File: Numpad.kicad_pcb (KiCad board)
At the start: 2 copper layers, 50 parts, among them J1 USB_B_Mini, SW0 MXSwitch, SW1 MXSwitch, SW2 MXSwitch, SW3 MXSwitch, SW4 MXSwitch, SW5 MXSwitch, SW6 MXSwitch, SW7 MXSwitch, SW8 MXSwitch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

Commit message: Components roughly placed in grid, connected rows and cols to processor
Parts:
- moved SWPls1 171.3 mm to (256.5, 80.6)
- moved SWEnt1 171.2 mm to (256.5, 118.7)
- moved C4 167.6 mm to (65.4, -31.1)
- moved C1 134.6 mm to (102.9, -24.1)
- moved C2 134.6 mm to (97.1, -17.4)
- moved C3 134.6 mm to (128.7, -49.6)
- moved C5 134.6 mm to (139.8, -61.1)
- moved C6 134.6 mm to (123.0, -42.9)
- moved C7 134.6 mm to (162.2, -81.2)
- moved J1 134.6 mm to (126.2, -63.5)
- moved R1 134.6 mm to (20.9, -1.16)
- moved R2 134.6 mm to (52.6, -1.91)
- moved R3 134.6 mm to (46.7, -1.91)
- moved R4 134.6 mm to (40.7, -1.91)
- moved SWRst1 134.6 mm to (33.0, -4.28)
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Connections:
- U1 pad 10: Net-(U1-Pad10) -> Row3
- U1 pad 11: Net-(U1-Pad11) -> Row4
- U1 pad 18: Net-(U1-Pad18) -> Col1
- U1 pad 19: Net-(U1-Pad19) -> Col2
- U1 pad 20: Net-(U1-Pad20) -> Col3
- U1 pad 21: Net-(U1-Pad21) -> Col4
- U1 pad 28: Net-(U1-Pad28) -> Row5
- U1 pad 8: Net-(U1-Pad8) -> Row1
- U1 pad 9: Net-(U1-Pad9) -> Row2

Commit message: components roughly placed
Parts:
- added H1: MountingHole, MountingHole:MountingHole_3mm_Pad, F.Cu at (189.9, 61.6)
- added H2: MountingHole, MountingHole:MountingHole_3mm_Pad, F.Cu at (189.9, 118.7)
- added H3: MountingHole, MountingHole:MountingHole_3mm_Pad, F.Cu at (228.0, 61.6)
- added H4: MountingHole, MountingHole:MountingHole_3mm_Pad, F.Cu at (228.0, 118.7)
- Y1: footprint Crystal:Crystal_SMD_5032-2Pin_5.0x3.2mm_HandSoldering -> Crystal:Crystal_SMD_3225-4Pin_3.2x2.5mm_HandSoldering
- moved SWRst1 221.9 mm to (211.5, 127.6)
- moved Y1 213.4 mm to (208.9, 99.7), turned to 180 degrees
- moved R1 209.2 mm to (182.2, 132.1), turned to 270 degrees
- moved R3 179.0 mm to (214.0, 61.6), turned to 180 degrees
- moved R4 175.6 mm to (204.5, 61.6), turned to 180 degrees
- moved C1 174.4 mm to (177.8, 133.3), turned to 180 degrees
- moved C3 173.9 mm to (208.9, 104.8)
- moved C2 158.3 mm to (208.9, 94.6)
- moved U1 150.2 mm to (180.3, 99.7), turned to 90 degrees
- moved R2 146.8 mm to (180.3, 70.5), turned to 180 degrees
- moved C4 146.1 mm to (190.5, 44.5)
- moved C7 143.9 mm to (207.6, 55.2), turned to 90 degrees
- moved J1 137.5 mm to (208.9, 46.4), turned to 180 degrees
- moved C5 137.3 mm to (212.7, 55.2), turned to 90 degrees
- moved DNum1 134.7 mm to (244.5, 55.2), turned to 90 degrees
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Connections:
- net Net-(R2-Pad1) renamed D+
- net Net-(R3-Pad1) renamed D-
- Y1 pad 2: Net-(C3-Pad1) -> GND

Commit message: ignore bak files, went bak to standard pcb orientation
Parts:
- added R5: 330, Resistor_SMD:R_1206_3216Metric_Pad1.42x1.75mm_HandSolder, F.Cu at (50.8, 58.4)
- D0, D1, D2, D3, D4, D5, D6, D7, D8, D9, DAst1, DDel1, DDiv1, DEnt1, DNum1, DPls1: value D_Small -> 1N4148W
- R4: value 10K -> 1K
- moved C7 191.4 mm to (16.5, 45.7)
- moved SWRst1 191.4 mm to (20.3, 118.1)
- moved C2 191.4 mm to (17.8, 85.1)
- moved C3 191.4 mm to (17.8, 95.2)
- moved C5 191.4 mm to (21.6, 45.7)
- moved C6 191.4 mm to (19.1, 45.7)
- moved C8 191.4 mm to (14.0, 45.7)
- moved D3 191.4 mm to (15.2, 102.9)
- moved J1 191.4 mm to (17.8, 36.8)
- moved R3 191.4 mm to (22.9, 52.1)
- moved R4 191.4 mm to (13.3, 52.1)
- moved Y1 191.4 mm to (17.8, 90.2)
- moved DNum1 151.8 mm to (92.7, 52.7)
- moved DDiv1 149.9 mm to (75.6, 50.2)
- moved D0 143.6 mm to (91.4, 125.7)
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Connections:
- C1 pad 2: GND -> Net-(C1-Pad2)
- SWRst1 pad 2: GND -> Net-(C1-Pad2)

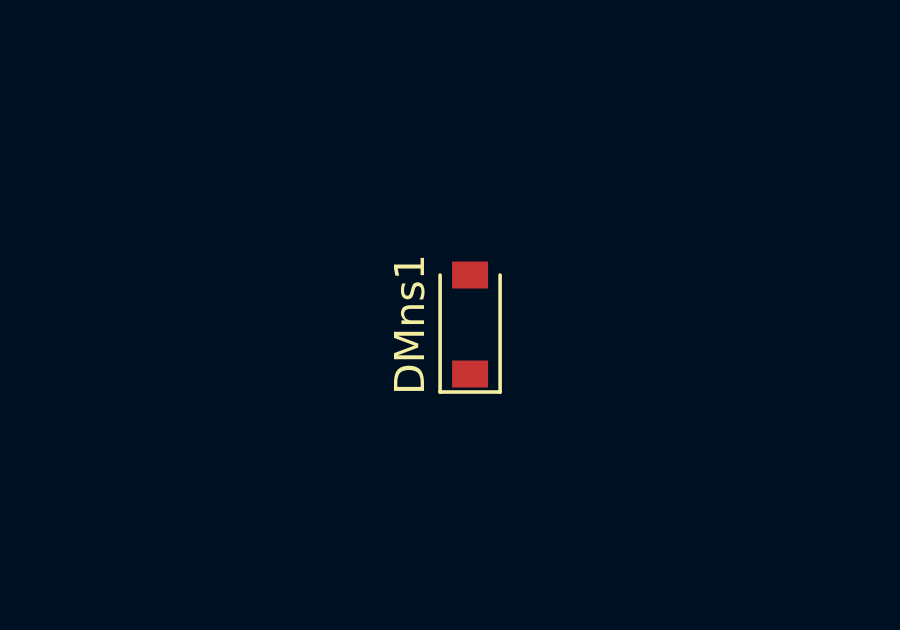
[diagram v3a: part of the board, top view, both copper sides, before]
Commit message: MX labels updated, missed diode spec
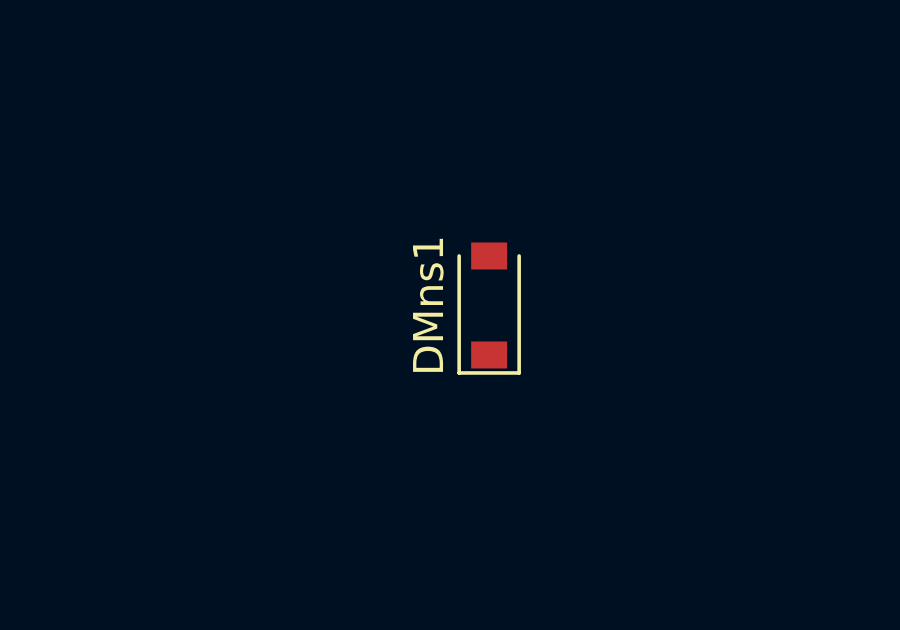
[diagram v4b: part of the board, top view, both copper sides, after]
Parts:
- DMns1: value D_Small -> 1N4148W
- SW0: value MXSwitch -> 0
- SW1: value MXSwitch -> 1
- SW2: value MXSwitch -> 2
- SW3: value MXSwitch -> 3
- SW4: value MXSwitch -> 4
- SW5: value MXSwitch -> 5
- SW6: value MXSwitch -> 6
- SW7: value MXSwitch -> 7
- SW8: value MXSwitch -> 8
- SW9: value MXSwitch -> 9
- SWAst1: value MXSwitch -> *
- SWDel1: value MXSwitch -> Del
- SWDiv1: value MXSwitch -> /
- SWEnt1: value MXSwitch -> Ent
- SWMns1: value MXSwitch -> -
- SWNum1: value MXSwitch -> Num
- SWPls1: value MXSwitch -> +
- moved DMns1 0.90 mm to (123.8, 53.3)
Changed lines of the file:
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@@
   (module AcheronMX:MX200V (layer F.Cu)
     (at 248.92 76.835)
-    (fp_text reference SWPls1 (at 0 3.175) (layer Cmts.User)
-      (effects (font (size 1 1) (thickness 0.15) italic))
-    )
-    (fp_text value MXSwitch (at 0 8.7) (layer Cmts.User)
+    (fp_text reference SWPls1 (at 0 3.175) (layer Cmts.User) hide
+      (effects (font (size 1 1) (thickness 0.15) italic))
+    )
+    (fp_text value + (at 0 8.7) (layer Cmts.User)
       (effects (font (size 1 1) (thickness 0.15)))
     )
@@
   (module AcheronMX:MX100 (layer F.Cu)
     (at 191.77 48.26)
-    (fp_text reference SWNum1 (at 0 3.175) (layer Cmts.User)
-      (effects (font (size 1 1) (thickness 0.15) italic))
-    )
-    (fp_text value MXSwitch (at 0 8.636) (layer Cmts.User)
+    (fp_text reference SWNum1 (at 0 3.175) (layer Cmts.User) hide
+      (effects (font (size 1 1) (thickness 0.15) italic))
+    )
+    (fp_text value Num (at 0 8.636) (layer Cmts.User)
       (effects (font (size 1 1) (thickness 0.15)))
     )
@@
   (module AcheronMX:MX100 (layer F.Cu)
     (at 248.92 48.26)
-    (fp_text reference SWMns1 (at 0 3.175) (layer Cmts.User)
-      (effects (font (size 1 1) (thickness 0.15) italic))
-    )
-    (fp_text value MXSwitch (at 0 8.636) (layer Cmts.User)
+    (fp_text reference SWMns1 (at 0 3.175) (layer Cmts.User) hide
+      (effects (font (size 1 1) (thickness 0.15) italic))
+    )
+    (fp_text value - (at 0 8.636) (layer Cmts.User)
       (effects (font (size 1 1) (thickness 0.15)))
     )
@@
   (module AcheronMX:MX200V (layer F.Cu)
     (at 248.92 114.935)
-    (fp_text reference SWEnt1 (at 0 3.175) (layer Cmts.User)
-      (effects (font (size 1 1) (thickness 0.15) italic))
-    )
-    (fp_text value MXSwitch (at 0 8.7) (layer Cmts.User)
+    (fp_text reference SWEnt1 (at 0 3.175) (layer Cmts.User) hide
+      (effects (font (size 1 1) (thickness 0.15) italic))
+    )
+    (fp_text value Ent (at 0 8.7) (layer Cmts.User)
       (effects (font (size 1 1) (thickness 0.15)))
     )
@@
   (module AcheronMX:MX100 (layer F.Cu)
     (at 210.82 48.26)
-    (fp_text reference SWDiv1 (at 0 3.175) (layer Cmts.User)
-      (effects (font (size 1 1) (thickness 0.15) italic))
-    )
-    (fp_text value MXSwitch (at 0 8.636) (layer Cmts.User)
+    (fp_text reference SWDiv1 (at 0 3.175) (layer Cmts.User) hide
+      (effects (font (size 1 1) (thickness 0.15) italic))
+    )
+    (fp_text value / (at 0 8.636) (layer Cmts.User)
       (effects (font (size 1 1) (thickness 0.15)))
     )
@@
   (module AcheronMX:MX100 (layer F.Cu)
     (at 229.87 124.46)
-    (fp_text reference SWDel1 (at 0 3.175) (layer Cmts.User)
-      (effects (font (size 1 1) (thickness 0.15) italic))
-    )
-    (fp_text value MXSwitch (at 0 8.636) (layer Cmts.User)
+    (fp_text reference SWDel1 (at 0 3.175) (layer Cmts.User) hide
+      (effects (font (size 1 1) (thickness 0.15) italic))
+    )
+    (fp_text value Del (at 0 8.636) (layer Cmts.User)
       (effects (font (size 1 1) (thickness 0.15)))
     )
@@
   (module AcheronMX:MX100 (layer F.Cu)
     (at 229.87 48.26)
-    (fp_text reference SWAst1 (at 0 3.175) (layer Cmts.User)
-      (effects (font (size 1 1) (thickness 0.15) italic))
-    )
-    (fp_text value MXSwitch (at 0 8.636) (layer Cmts.User)
+    (fp_text reference SWAst1 (at 0 3.175) (layer Cmts.User) hide
+      (effects (font (size 1 1) (thickness 0.15) italic))
+    )
+    (fp_text value * (at 0 8.636) (layer Cmts.User)
       (effects (font (size 1 1) (thickness 0.15)))
     )
@@
       (effects (font (size 1 1) (thickness 0.15) italic))
     )
-    (fp_text value MXSwitch (at 0 8.636) (layer Cmts.User)
+    (fp_text value 9 (at 0 8.636) (layer Cmts.User)
       (effects (font (size 1 1) (thickness 0.15)))
     )
@@
   (module AcheronMX:MX100 (layer F.Cu)
     (at 210.82 67.31)
-    (fp_text reference SW8 (at 0 3.175) (layer Cmts.User)
-      (effects (font (size 1 1) (thickness 0.15) italic))
-    )
-    (fp_text value MXSwitch (at 0 8.636) (layer Cmts.User)
+    (fp_text reference SW8 (at 0 3.175) (layer Cmts.User) hide
+      (effects (font (size 1 1) (thickness 0.15) italic))
+    )
+    (fp_text value 8 (at 0 8.636) (layer Cmts.User)
       (effects (font (size 1 1) (thickness 0.15)))
     )
@@
   (module AcheronMX:MX100 (layer F.Cu)
     (at 191.77 67.31)
-    (fp_text reference SW7 (at 0 3.175) (layer Cmts.User)
-      (effects (font (size 1 1) (thickness 0.15) italic))
-    )
-    (fp_text value MXSwitch (at 0 8.636) (layer Cmts.User)
+    (fp_text reference SW7 (at 0 3.175) (layer Cmts.User) hide
+      (effects (font (size 1 1) (thickness 0.15) italic))
+    )
+    (fp_text value 7 (at 0 8.636) (layer Cmts.User)
       (effects (font (size 1 1) (thickness 0.15)))
     )
@@
   (module AcheronMX:MX100 (layer F.Cu)
     (at 229.87 86.36)
-    (fp_text reference SW6 (at 0 3.175) (layer Cmts.User)
-      (effects (font (size 1 1) (thickness 0.15) italic))
-    )
-    (fp_text value MXSwitch (at 0 8.636) (layer Cmts.User)
+    (fp_text reference SW6 (at 0 3.175) (layer Cmts.User) hide
+      (effects (font (size 1 1) (thickness 0.15) italic))
+    )
+    (fp_text value 6 (at 0 8.636) (layer Cmts.User)
       (effects (font (size 1 1) (thickness 0.15)))
     )
@@
   (module AcheronMX:MX100 (layer F.Cu)
     (at 210.82 86.36)
-    (fp_text reference SW5 (at 0 3.175) (layer Cmts.User)
-      (effects (font (size 1 1) (thickness 0.15) italic))
-    )
-    (fp_text value MXSwitch (at 0 8.636) (layer Cmts.User)
+    (fp_text reference SW5 (at 0 3.175) (layer Cmts.User) hide
+      (effects (font (size 1 1) (thickness 0.15) italic))
+    )
+    (fp_text value 5 (at 0 8.636) (layer Cmts.User)
       (effects (font (size 1 1) (thickness 0.15)))
     )
@@
   (module AcheronMX:MX100 (layer F.Cu)
     (at 191.77 86.36)
-    (fp_text reference SW4 (at 0 3.175) (layer Cmts.User)
-      (effects (font (size 1 1) (thickness 0.15) italic))
-    )
-    (fp_text value MXSwitch (at 0 8.636) (layer Cmts.User)
+    (fp_text reference SW4 (at 0 3.175) (layer Cmts.User) hide
+      (effects (font (size 1 1) (thickness 0.15) italic))
+    )
+    (fp_text value 4 (at 0 8.636) (layer Cmts.User)
       (effects (font (size 1 1) (thickness 0.15)))
     )
@@
   (module AcheronMX:MX100 (layer F.Cu)
     (at 229.87 105.41)
-    (fp_text reference SW3 (at 0 3.175) (layer Cmts.User)
-      (effects (font (size 1 1) (thickness 0.15) italic))
-    )
-    (fp_text value MXSwitch (at 0 8.636) (layer Cmts.User)
+    (fp_text reference SW3 (at 0 3.175) (layer Cmts.User) hide
+      (effects (font (size 1 1) (thickness 0.15) italic))
+    )
+    (fp_text value 3 (at 0 8.636) (layer Cmts.User)
       (effects (font (size 1 1) (thickness 0.15)))
     )
@@
   (module AcheronMX:MX100 (layer F.Cu)
     (at 210.82 105.41)
-    (fp_text reference SW2 (at 0 3.175) (layer Cmts.User)
-      (effects (font (size 1 1) (thickness 0.15) italic))
-    )
-    (fp_text value MXSwitch (at 0 8.636) (layer Cmts.User)
+    (fp_text reference SW2 (at 0 3.175) (layer Cmts.User) hide
+      (effects (font (size 1 1) (thickness 0.15) italic))
+    )
+    (fp_text value 2 (at 0 8.636) (layer Cmts.User)
       (effects (font (size 1 1) (thickness 0.15)))
     )
@@
   (module AcheronMX:MX100 (layer F.Cu)
     (at 191.77 105.41)
-    (fp_text reference SW1 (at 0 3.175) (layer Cmts.User)
-      (effects (font (size 1 1) (thickness 0.15) italic))
-    )
-    (fp_text value MXSwitch (at 0 8.636) (layer Cmts.User)
+    (fp_text reference SW1 (at 0 3.175) (layer Cmts.User) hide
+      (effects (font (size 1 1) (thickness 0.15) italic))
+    )
+    (fp_text value 1 (at 0 8.636) (layer Cmts.User)
       (effects (font (size 1 1) (thickness 0.15)))
     )
@@
   (module AcheronMX:MX200 (layer F.Cu)
     (at 201.295 124.46)
-    (fp_text reference SW0 (at 0 3.175) (layer Cmts.User)
-      (effects (font (size 1 1) (thickness 0.15) italic))
-    )
-    (fp_text value MXSwitch (at 0 8.7) (layer Cmts.User)
+    (fp_text reference SW0 (at 0 3.175) (layer Cmts.User) hide
+      (effects (font (size 1 1) (thickness 0.15) italic))
+    )
+    (fp_text value 0 (at 0 8.7) (layer Cmts.User)
       (effects (font (size 1 1) (thickness 0.15)))
     )
@@
   )
   (module Diode_SMD:D_SOD-123 (layer F.Cu)
-    (at 123.19 53.975 90)
+    (at 123.825 53.34 90)
     (descr SOD-123)
     (tags SOD-123)
@@
       (effects (font (size 1 1) (thickness 0.15)))
     )
-    (fp_text value D_Small (at 0 2.1 90) (layer F.Fab)
-      (effects (font (size 1 1) (thickness 0.15)))
-    )
+    (fp_text value 1N4148W (at 0 2.1 90) (layer F.Fab)
+      (effects (font (size 1 1) (thickness 0.15)))
+    )

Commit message: rotated stabiliser holes for tighter pcb
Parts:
- SW0: footprint AcheronMX:MX200 -> AcheronMX:MX200R
- SWEnt1, SWPls1: footprint AcheronMX:MX200V -> AcheronMX:MX200VR
- moved J1 173.9 mm to (191.5, 45.0)
- moved SWEnt1 86.1 mm to (162.9, 117.2)
- moved SWMns1 86.1 mm to (162.9, 50.5)
- moved SWPls1 86.1 mm to (162.9, 79.1)
- moved H2 67.1 mm to (172.4, 117.2)
- moved SWAst1 48.0 mm to (181.9, 50.5)
- moved SWDel1 48.0 mm to (181.9, 126.7)
- moved SW3 48.0 mm to (181.9, 107.6)
- moved SW6 48.0 mm to (181.9, 88.6)
- moved SW9 48.0 mm to (181.9, 69.5)
- moved H1 35.9 mm to (210.5, 79.1)
- moved H3 35.9 mm to (172.4, 79.1)
- moved SW1 28.3 mm to (220.0, 107.6)
- moved SW4 28.3 mm to (220.0, 88.6)
- moved SW7 28.3 mm to (220.0, 69.5)
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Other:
- board outline added: 76.2 x 97.6 mm

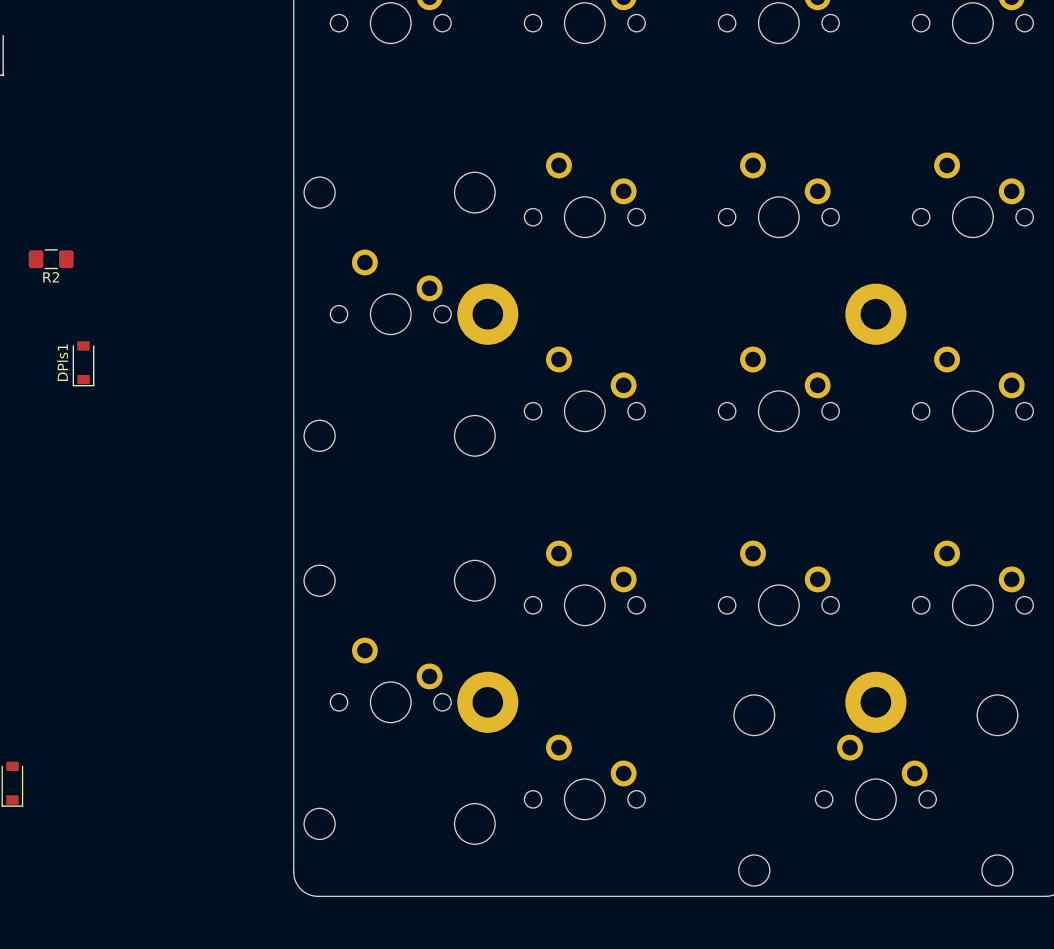
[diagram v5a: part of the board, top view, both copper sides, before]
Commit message: copied aio3's capacitor settings and fuse placement
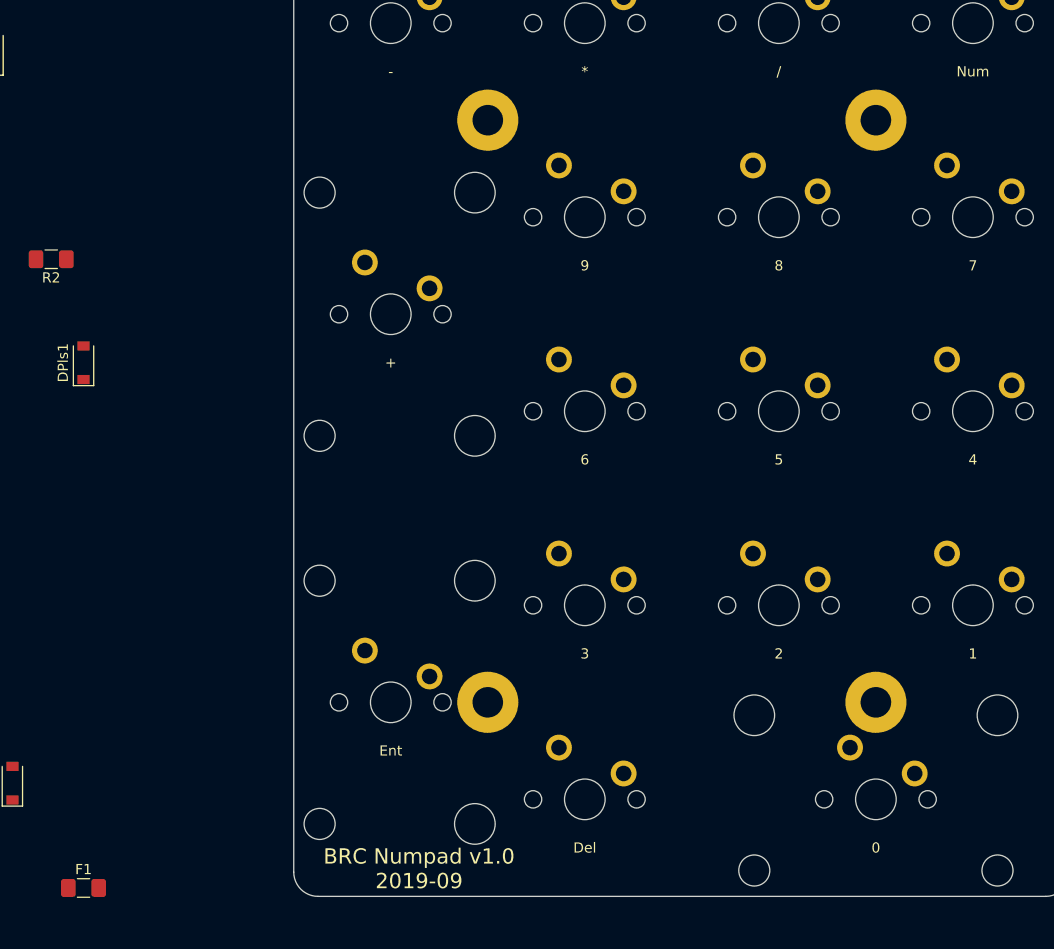
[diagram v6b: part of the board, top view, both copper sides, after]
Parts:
- added F1: 500mA, Fuse:Fuse_1206_3216Metric_Pad1.42x1.75mm_HandSolder, F.Cu at (132.7, 135.4)
- C6: value 1uF -> 0.1uF
- C7: value 100n -> 0.1uF
- C8: value 100n -> 01.uF
- R4: value 1K -> 10k
- moved H1 19.1 mm to (210.5, 60.0)
- moved H3 19.1 mm to (172.4, 60.0)
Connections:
- J1 pad 1: +5V -> VCC
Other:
- board text added: "BRC Numpad v1.0 2019-09"

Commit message: numpad name ben17
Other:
- board text added: "Ben17 Numpad v1.0 2019-09"
- board text removed: "BRC Numpad v1.0 2019-09"
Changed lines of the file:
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@@
     )
   )
-  (gr_text "BRC Numpad v1.0\n2019-09" (at 165.6588 133.5024) (layer F.SilkS)
+  (gr_text "Ben17 Numpad\nv1.0 2019-09" (at 165.6588 133.5024) (layer F.SilkS)
     (effects (font (size 1.5 1.5) (thickness 0.3)))
   )
